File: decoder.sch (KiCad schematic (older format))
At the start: 1 part

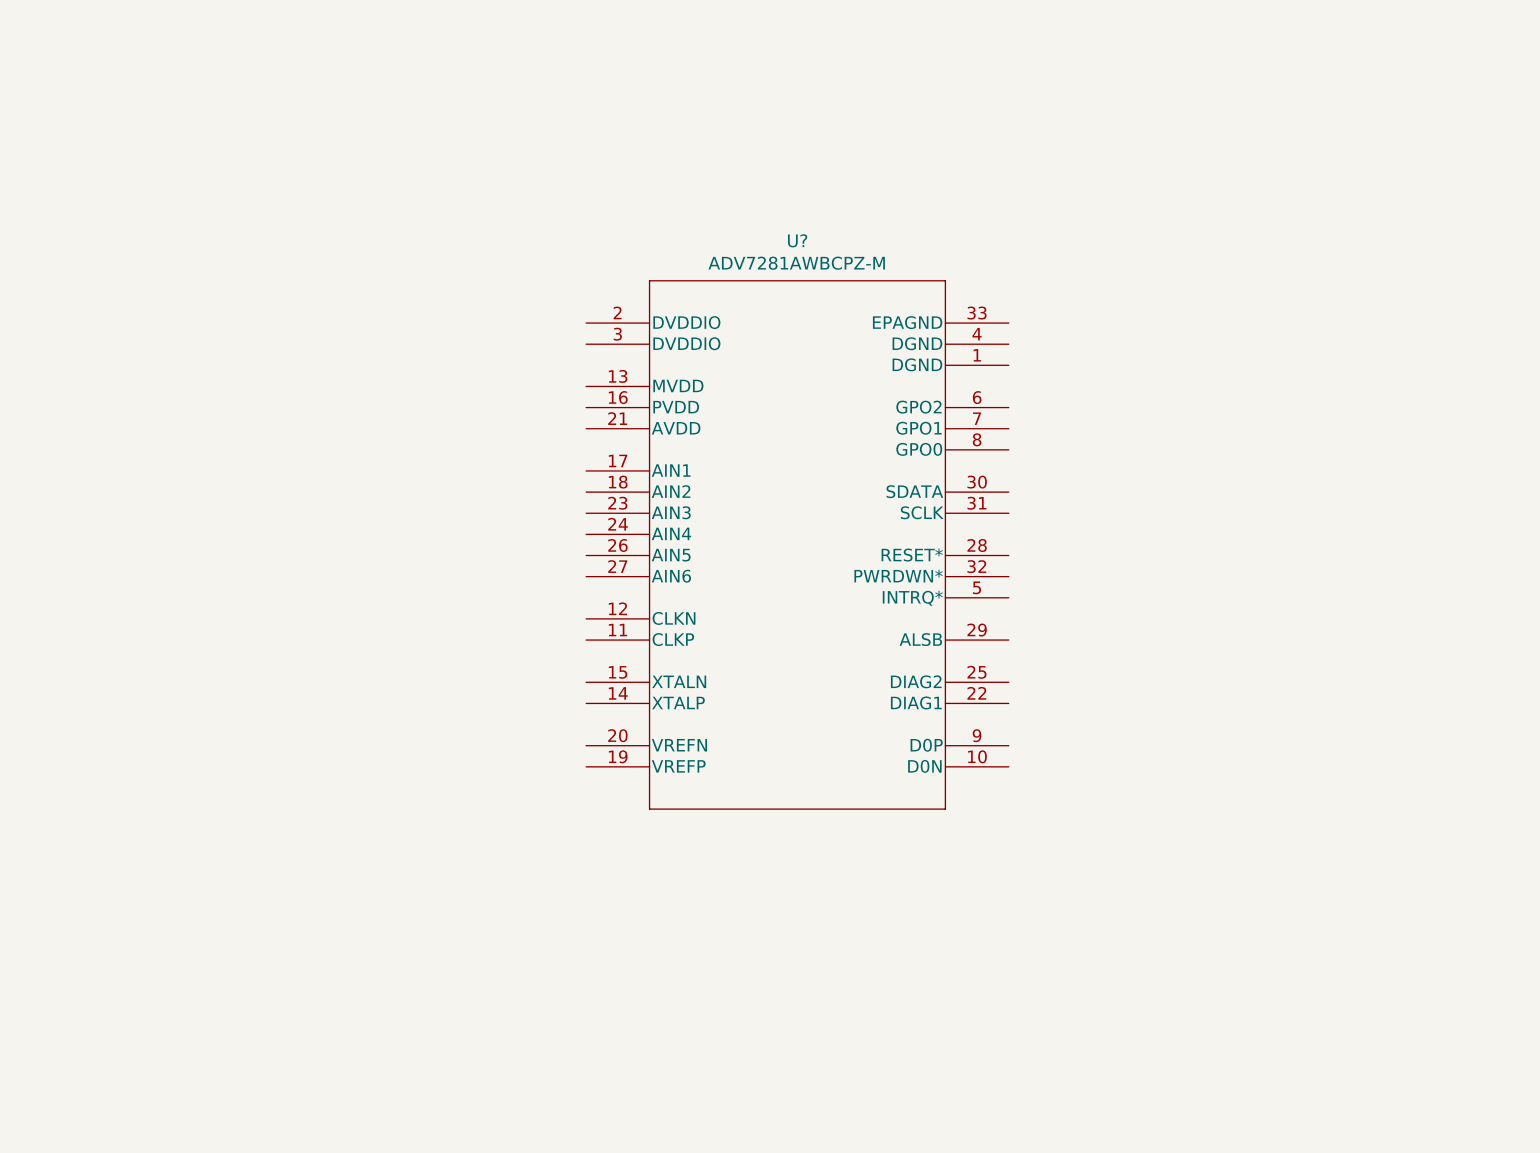
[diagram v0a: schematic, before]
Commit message: Add resistors and capacitors for the decoder
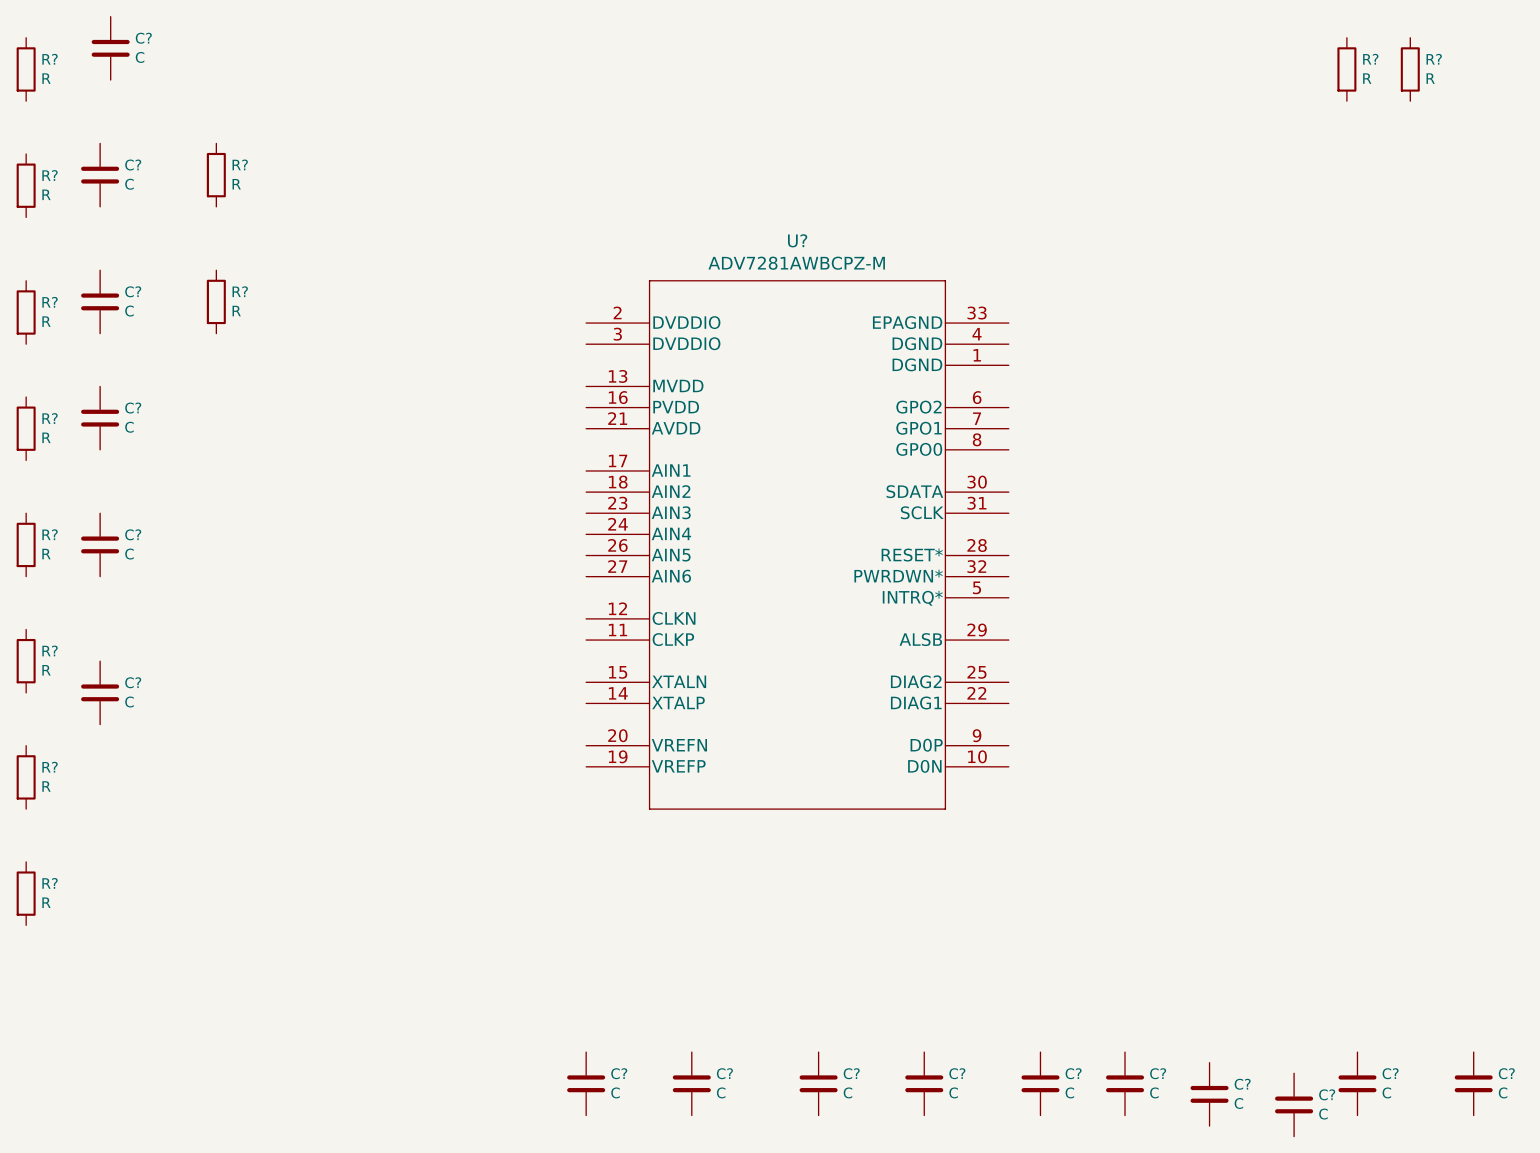
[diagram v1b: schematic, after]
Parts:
- added C? (x16): C, symbol Device:C
- added R? (x12): R, symbol Device:R
